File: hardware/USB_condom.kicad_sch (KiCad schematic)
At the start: 4 parts, among them J1 USB_A, J2 USB_A, U1 TPS2514A

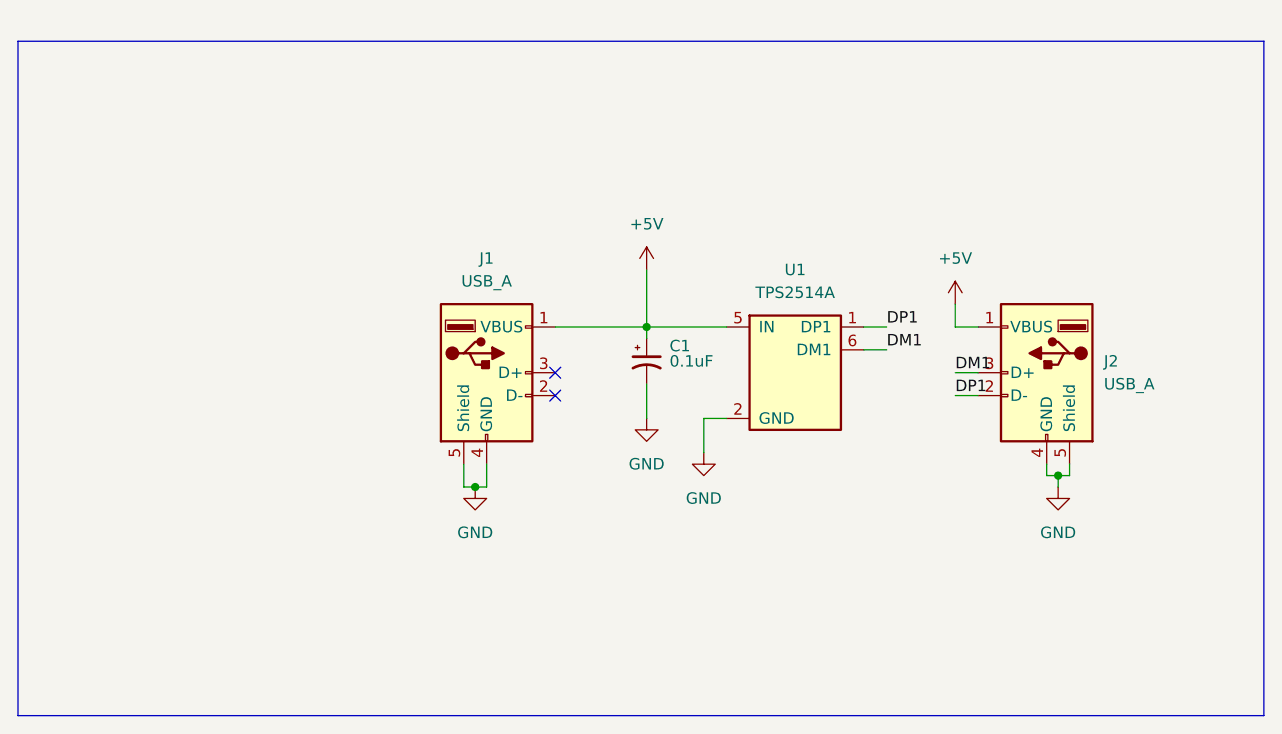
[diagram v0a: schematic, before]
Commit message: Usb a-a, usb a-b upgrade
Last update of the USB condom
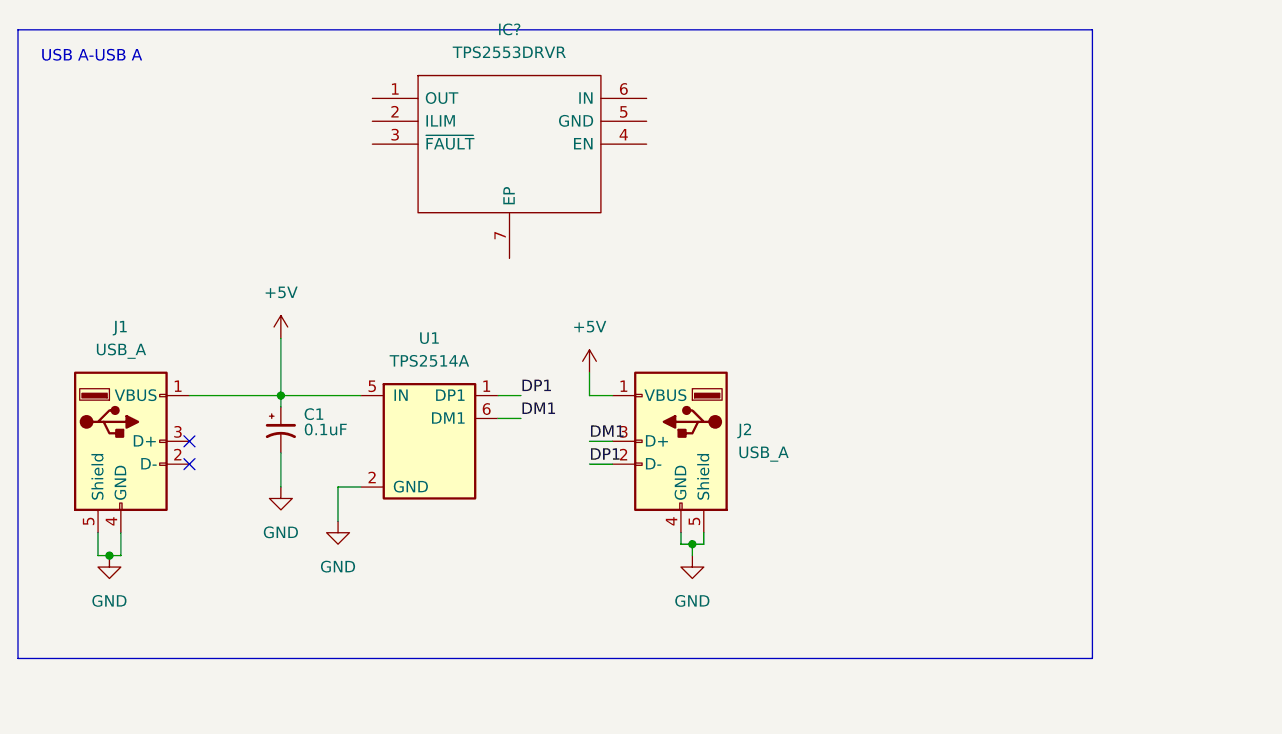
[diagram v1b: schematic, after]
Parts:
- added IC?: TPS2553DRVR, SON65P200X200X80-7N, symbol tps2533:TPS2553DRVR
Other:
- note added: "USB A-USB A"
- moved on the sheet: C1, J1, J2, U1

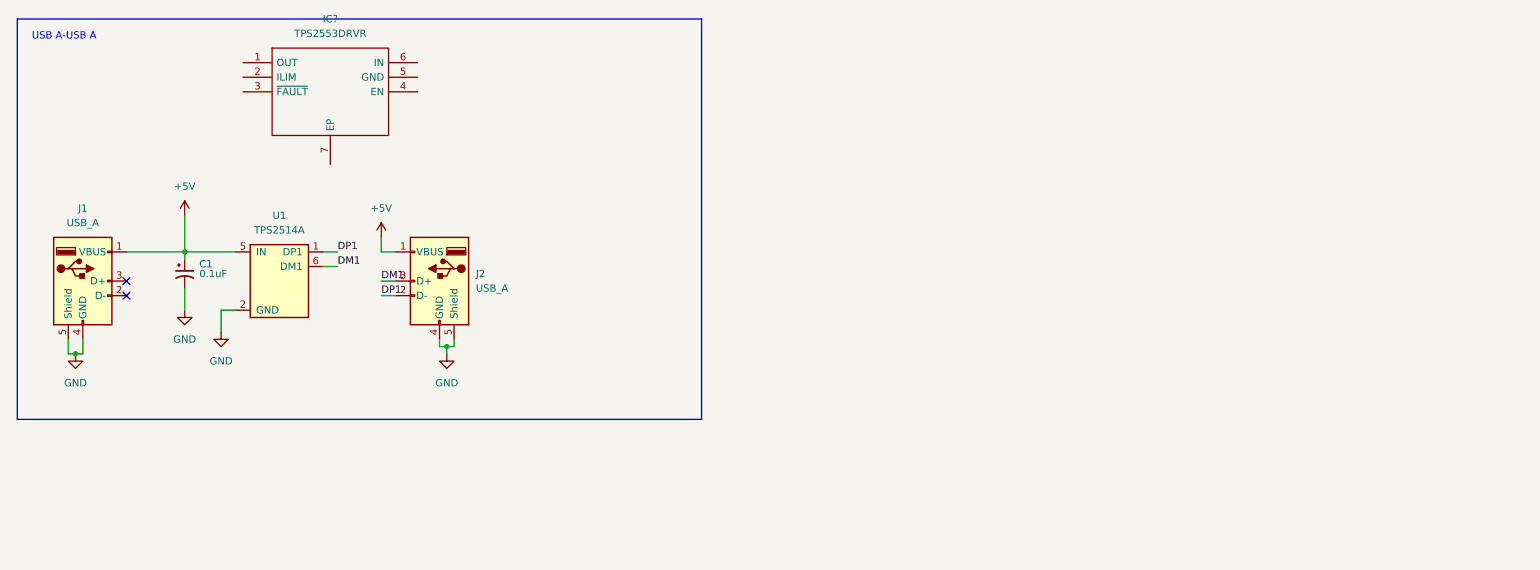
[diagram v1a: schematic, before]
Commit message: update project add schematic and first layout
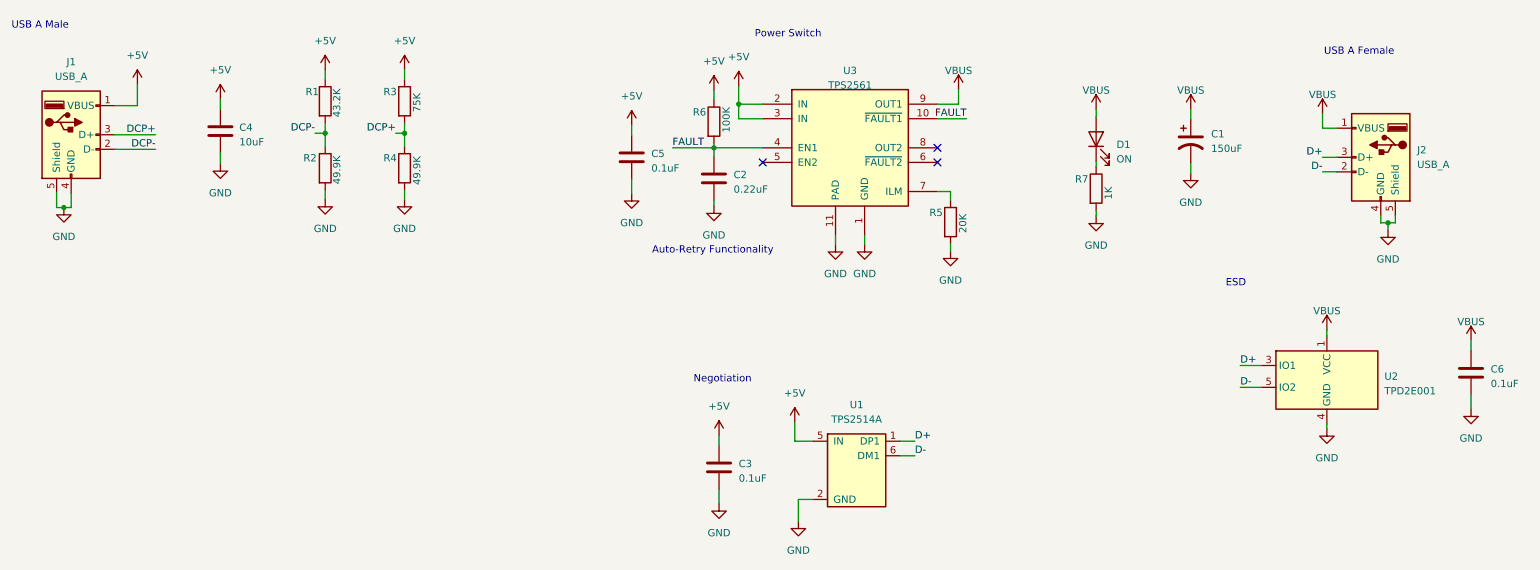
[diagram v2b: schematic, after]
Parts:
- removed C1: 0.1uF, Capacitor_SMD:C_0805_2012Metric, symbol Device:C_Polarized_Small_US
- removed IC?: TPS2553DRVR, SON65P200X200X80-7N, symbol tps2533:TPS2553DRVR
- added C1: 150uF, symbol Device:C_Polarized_US
- added C2: 0.22uF, Capacitor_SMD:C_0402_1005Metric, symbol Device:C
- added C3, C5, C6: 0.1uF, Capacitor_SMD:C_0402_1005Metric, symbol Device:C
- added C4: 10uF, Capacitor_SMD:C_0805_2012Metric, symbol Device:C
- added D1: ON, LED_SMD:LED_0402_1005Metric, symbol Device:LED
- added R1: 43.2K, Resistor_SMD:R_0402_1005Metric, symbol Device:R
- added R2, R4: 49.9K, Resistor_SMD:R_0402_1005Metric, symbol Device:R
- added R3: 75K, Resistor_SMD:R_0402_1005Metric, symbol Device:R
- added R5: 20K, Resistor_SMD:R_0402_1005Metric, symbol Device:R
- added R6: 100K, Resistor_SMD:R_0402_1005Metric, symbol Device:R
- added R7: 1K, Resistor_SMD:R_0402_1005Metric, symbol Device:R
- added U2: TPD2E001, Package_TO_SOT_SMD:SOT-553, symbol usbCondom:TPD2E001DRLR
- added U3: TPS2561, Package_SON:VSON-10-1EP_3x3mm_P0.5mm_EP1.65x2.4mm_ThermalVias, symbol Interface_USB:TPS2561
- J1: footprint Connector_USB:USB_A_Stewart_SS-52100-001_Horizontal -> usbCondom:C46394
- J2: footprint Connector_USB:USB_A_Stewart_SS-52100-001_Horizontal -> Connector_USB:USB_A_TE_292303-7_Horizontal
- U1: LCSC3 (none) -> C157567; manf# (none) -> TPS2514ADBVR
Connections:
- net +5V: now also C3.1, C4.1, C5.1, R1.1, R3.1, R6.1, U3.2 (IN), U3.3 (IN); no longer J2.1 (VBUS)
- net GND: now also C1.2, C2.2, C3.2, C4.2, C5.2, C6.2, R2.2, R4.2, R5.2, R7.2, U2.4 (GND), U3.1 (GND), U3.11 (PAD)
- net DCP-: now reaches J1.2 (D-)
- net DCP-: now also R1.2, R2.1
- net DCP+: now reaches J1.3 (D+)
- net DCP+: now also R3.2, R4.1
- net DM1 renamed D+
- net D+: now also U1.1 (DP1), U2.3 (IO1); no longer U1.6 (DM1)
- net DP1 renamed D-
- net D-: now also U1.6 (DM1), U2.5 (IO2); no longer U1.1 (DP1)
- new net: D1.1 (K), R7.1
- new net: R5.1, U3.7 (ILM)
- new net FAULT: C2.1, R6.2, U3.10 (~{FAULT1}), U3.4 (EN1)
- new net VBUS: C1.1, C6.1, D1.2 (A), J2.1 (VBUS), U2.1 (VCC), U3.9 (OUT1)
- no-connect marks 2 -> 3
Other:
- note added: "Auto-Retry Functionality"
- note added: "ESD"
- note added: "Negotiation"
- note added: "Power Switch"
- note added: "USB A Female"
- note added: "USB A Male"
- note removed: "USB A-USB A"
- moved on the sheet: J1, J2, U1

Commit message: add capacitor, add LCSC numbers
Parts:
- C1: footprint (none) -> Capacitor_SMD:CP_Elec_6.3x5.4; LCSC# (none) -> C2895744
- C2: LCSC# (none) -> C2903665
- C3, C5, C6: LCSC# (none) -> C392963
- C4: LCSC# (none) -> C3015160
- D1: LCSC# (none) -> C965790
- J1: LCSC# (none) -> C46394
- J2: footprint Connector_USB:USB_A_TE_292303-7_Horizontal -> usbCondom:875832010BLF; LCSC# (none) -> C599118
- R1: LCSC# (none) -> C5356145
- R2, R4: LCSC# (none) -> C2906873
- R3: LCSC# (none) -> C3152096
- R5: LCSC# (none) -> C100292
- R6: LCSC# (none) -> C3152099
- R7: LCSC# (none) -> C3152067
- U1: LCSC# (none) -> C157567; LCSC3 C157567 -> (none)
- U3: manf# (none) -> TPS2561ADRCR
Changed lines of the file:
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@@
+      (effects (font (size 1.27 1.27)) hide)
+    )
+    (property "LCSC#" "C965790" (at 202.184 34.925 0)
       (effects (font (size 1.27 1.27)) hide)
     )
@@
       (effects (font (size 1.27 1.27)) hide)
     )
+    (property "LCSC#" "C2906873" (at 81.534 40.005 0)
+      (effects (font (size 1.27 1.27)) hide)
+    )
     (pin "1")
     (pin "2")
@@
       (effects (font (size 1.27 1.27)) hide)
     )
+    (property "LCSC#" "C3015160" (at 49.403 33.528 0)
+      (effects (font (size 1.27 1.27)) hide)
+    )
     (pin "1")
     (pin "2")
@@
       (effects (font (size 1.27 1.27)) hide)
     )
+    (property "LCSC#" "C392963" (at 136.398 92.202 0)
+      (effects (font (size 1.27 1.27)) hide)
+    )
     (pin "1")
     (pin "2")
@@
       (effects (font (size 1.27 1.27)) hide)
     )
+    (property "LCSC#" "C392963" (at 267.589 75.692 0)
+      (effects (font (size 1.27 1.27)) hide)
+    )
     (pin "1")
     (pin "2")
@@
     )
     (property "Datasheet" "~" (at 121.158 38.1 0)
+      (effects (font (size 1.27 1.27)) hide)
+    )
+    (property "LCSC#" "C392963" (at 121.158 38.1 0)
       (effects (font (size 1.27 1.27)) hide)
     )
@@
       (effects (font (size 1.27 1.27)) hide)
     )
+    (property "LCSC#" "C100292" (at 176.784 49.403 0)
+      (effects (font (size 1.27 1.27)) hide)
+    )
     (pin "1")
     (pin "2")
@@
       (effects (font (size 1.27 1.27)) (justify left))
     )
-    (property "Footprint" "" (at 218.694 35.306 0)
+    (property "Footprint" "Capacitor_SMD:CP_Elec_6.3x5.4" (at 218.694 35.306 0)
       (effects (font (size 1.27 1.27)) hide)
     )
@@
       (effects (font (size 1.27 1.27)) hide)
     )
+    (property "LCSC#" "C2895744" (at 218.694 35.306 0)
+      (effects (font (size 1.27 1.27)) hide)
+    )
     (pin "1")
     (pin "2")
@@
       (effects (font (size 1.27 1.27)) hide)
     )
-    (property "LCSC3" "C157567" (at 160.401 92.71 0)
+    (property "LCSC#" "C157567" (at 160.401 92.71 0)
       (effects (font (size 1.27 1.27)) hide)
     )
@@
       (effects (font (size 1.27 1.27)) hide)
     )
+    (property "LCSC#" "C2903665" (at 135.509 41.783 0)
+      (effects (font (size 1.27 1.27)) hide)
+    )
     (pin "1")
     (pin "2")
@@
       (effects (font (size 1.27 1.27)) hide)
     )
+    (property "LCSC#" "C5356145" (at 67.691 28.321 0)
+      (effects (font (size 1.27 1.27)) hide)
+    )
     (pin "1")
     (pin "2")
@@
     )
     (property "Datasheet" "http://www.ti.com/lit/ds/symlink/tps2561.pdf" (at 149.098 23.749 0)
+      (effects (font (size 1.27 1.27)) hide)
+    )
+    (property "manf#" "TPS2561ADRCR" (at 159.258 36.449 0)
       (effects (font (size 1.27 1.27)) hide)
     )
@@
       (effects (font (size 1.27 1.27)) hide)
     )
+    (property "LCSC#" "C3152067" (at 202.184 43.561 0)
+      (effects (font (size 1.27 1.27)) hide)
+    )
     (pin "1")
     (pin "2")
@@
       (effects (font (size 1.27 1.27)) hide)
     )
+    (property "LCSC#" "C3152099" (at 135.509 31.877 0)
+      (effects (font (size 1.27 1.27)) hide)
+    )
     (pin "1")
     (pin "2")
@@
       (effects (font (size 1.27 1.27)) hide)
     )
+    (property "LCSC#" "C3152096" (at 81.534 28.321 0)
+      (effects (font (size 1.27 1.27)) hide)
+    )
     (pin "1")
     (pin "2")
@@
     )
     (property "Datasheet" " ~" (at 27.178 35.433 0)
+      (effects (font (size 1.27 1.27)) hide)
+    )
+    (property "LCSC#" "C46394" (at 23.368 34.163 0)
       (effects (font (size 1.27 1.27)) hide)
     )
@@
       (effects (font (size 1.27 1.27)) hide)
     )
+    (property "LCSC#" "C2906873" (at 67.691 40.005 0)
+      (effects (font (size 1.27 1.27)) hide)
+    )
     (pin "1")
     (pin "2")
@@
       (effects (font (size 1.27 1.27)) (justify right))
     )
-    (property "Footprint" "Connector_USB:USB_A_TE_292303-7_Horizontal" (at 248.031 39.37 0)
+    (property "Footprint" "usbCondom:875832010BLF" (at 248.031 39.37 0)
       (effects (font (size 1.27 1.27)) hide)
     )
@@
       (effects (font (size 1.27 1.27)) hide)
     )
+    (property "LCSC#" "C599118" (at 251.841 38.1 0)
+      (effects (font (size 1.27 1.27)) hide)
+    )

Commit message: BOM updated
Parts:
- C2: LCSC# C2903665 -> C576742
- R1: LCSC# C5356145 -> C2906870
- R3: LCSC# C3152096 -> C328330
- R6: LCSC# C3152099 -> C284273
- R7: LCSC# C3152067 -> C2935237
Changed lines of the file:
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@@
       (effects (font (size 1.27 1.27)) hide)
     )
-    (property "LCSC#" "C2903665" (at 135.509 41.783 0)
+    (property "LCSC#" "C576742" (at 135.509 41.783 0)
       (effects (font (size 1.27 1.27)) hide)
     )
@@
       (effects (font (size 1.27 1.27)) hide)
     )
-    (property "LCSC#" "C5356145" (at 67.691 28.321 0)
+    (property "LCSC#" "C2906870" (at 67.691 28.321 0)
       (effects (font (size 1.27 1.27)) hide)
     )
@@
       (effects (font (size 1.27 1.27)) hide)
     )
-    (property "LCSC#" "C3152067" (at 202.184 43.561 0)
+    (property "LCSC#" "C2935237" (at 202.184 43.561 0)
       (effects (font (size 1.27 1.27)) hide)
     )
@@
       (effects (font (size 1.27 1.27)) hide)
     )
-    (property "LCSC#" "C3152099" (at 135.509 31.877 0)
+    (property "LCSC#" "C284273" (at 135.509 31.877 0)
       (effects (font (size 1.27 1.27)) hide)
     )
@@
       (effects (font (size 1.27 1.27)) hide)
     )
-    (property "LCSC#" "C3152096" (at 81.534 28.321 0)
-      (effects (font (size 1.27 1.27)) hide)
-    )
+    (property "LCSC#" "C328330" (at 81.534 28.321 0)
+      (effects (font (size 1.27 1.27)) hide)
+    )
